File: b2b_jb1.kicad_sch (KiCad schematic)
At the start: 11 parts, among them SW1 SDA02H1SBDR

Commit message: edit README.md
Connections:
- net CLK3+ is gone; now on net CLK1+: JB1.95 (F16|B35|T0|AD0P|L1P)
- net CLK3- is gone; now on net CLK1-: JB1.93 (E16|B35|T0|AD0N|L1N)
- net CNV3+ is gone; now on net CNV1+: JB1.99 (H19|B35|T3|L19P)
- net CNV3- is gone; now on net CNV1-: JB1.97 (H20|B35|T3|VREF|L19N)
- net DA3+ is gone; now on net DA1+: JB1.81 (E15|B35|T0|DQS|AD1P|L3P)
- net DA3- is gone; now on net DA1-: JB1.79 (D15|B35|T0|DQS|AD1N|L3N)
- net DB3+ is gone; now on net DB1+: JB1.77 (F18|B35|T0|AD9P|L5P)
- net DB3- is gone; now on net DB1-: JB1.75 (E18|B35|T0|AD9N|L5N)
- net DCO3+ is gone; now on net DCO1+: JB1.87 (G17|B35|T0|L6P)
- net DCO3- is gone; now on net DCO1-: JB1.85 (F17|B35|T0|VREF|L6N)
- net CLK1+: no longer JB1.66 (C20|B35|T2|AD4N|SRCC|L14N)
- net CLK1-: no longer JB1.68 (D20|B35|T2|AD4P|SRCC|L14P)
- net CNV1+: no longer JB1.60 (B20|B35|T2|MRCC|L13N)
- net CNV1-: no longer JB1.62 (B19|B35|T2|MRCC|L13P)
- net DA1+: no longer JB1.76 (C19|B35|T1|MRCC|L12N)
- net DA1-: no longer JB1.78 (D18|B35|T1|MRCC|L12P)
- net DB1+: no longer JB1.82 (F19|B35|T3|AD6N|L20N)
- net DB1-: no longer JB1.84 (G19|B35|T3|AD6P|L20P)
- net DCO1+: no longer JB1.70 (G16|B35|T0|L4N)
- net DCO1-: no longer JB1.72 (G15|B35|T0|L4P)
- new net CLK0+: JB1.66 (C20|B35|T2|AD4N|SRCC|L14N)
- new net CLK0-: JB1.68 (D20|B35|T2|AD4P|SRCC|L14P)
- new net CNV0+: JB1.60 (B20|B35|T2|MRCC|L13N)
- new net CNV0-: JB1.62 (B19|B35|T2|MRCC|L13P)
- new net DA0+: JB1.76 (C19|B35|T1|MRCC|L12N)
- new net DA0-: JB1.78 (D18|B35|T1|MRCC|L12P)
- new net DB0+: JB1.82 (F19|B35|T3|AD6N|L20N)
- new net DB0-: JB1.84 (G19|B35|T3|AD6P|L20P)
- new net DCO0+: JB1.70 (G16|B35|T0|L4N)
- new net DCO0-: JB1.72 (G15|B35|T0|L4P)
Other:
- company: (none) -> NOIRLab
- title: (none) -> 4 channel ADC Module

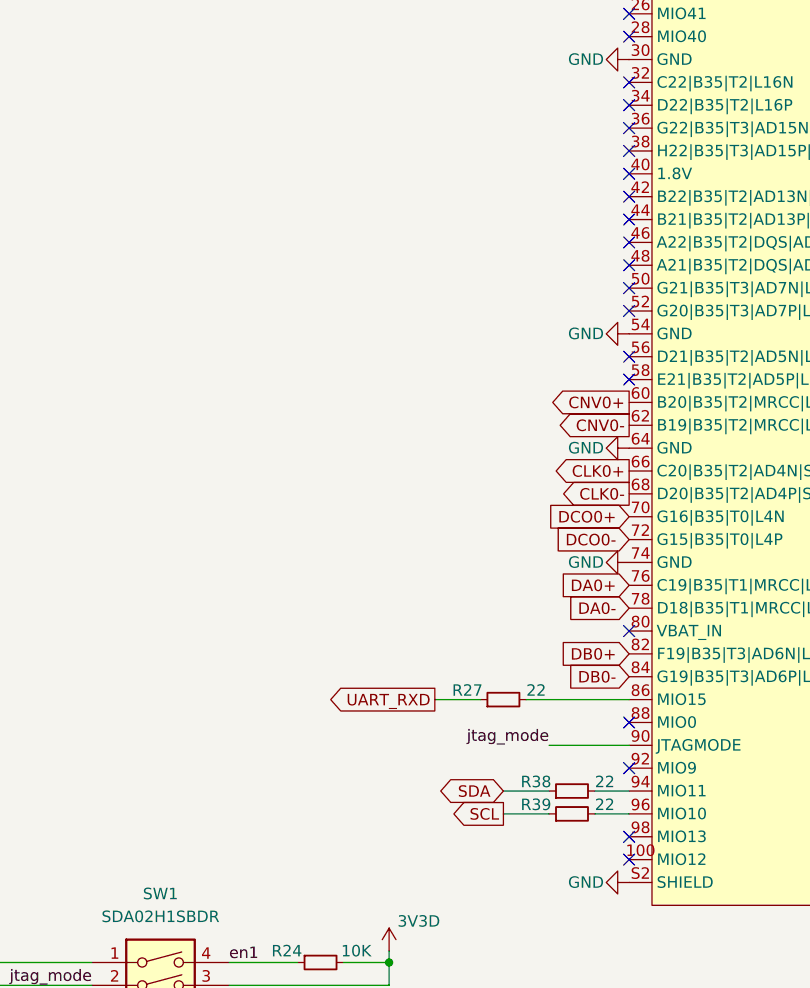
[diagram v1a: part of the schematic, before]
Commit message: Added clock sync and fix minor errors.
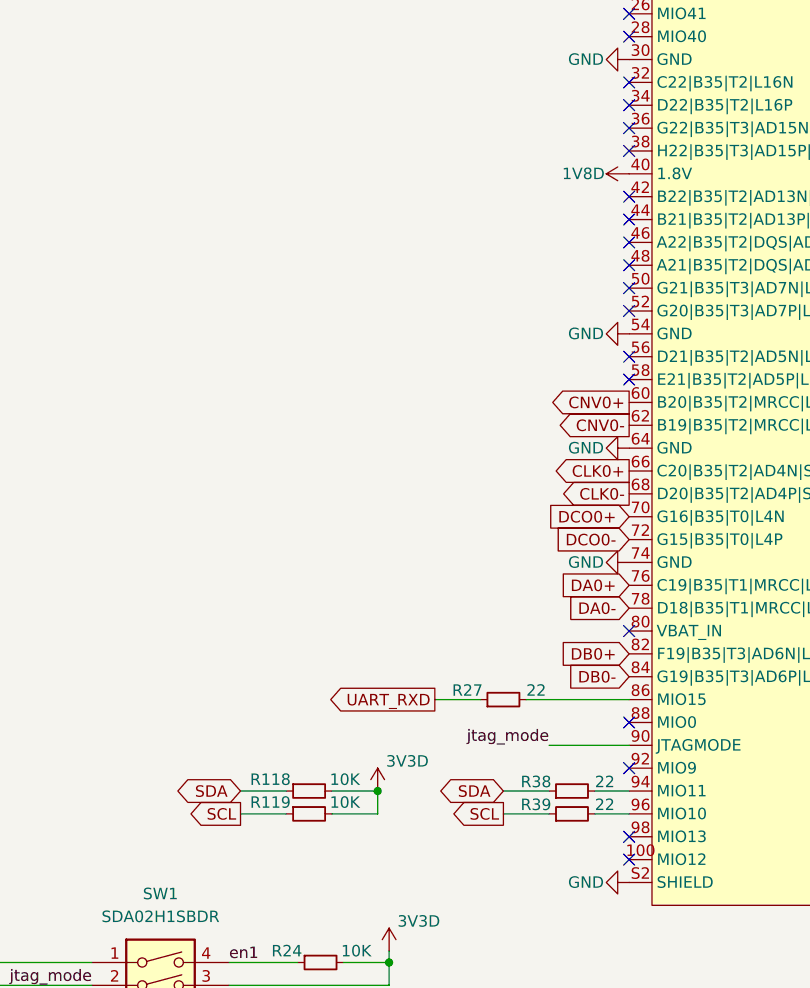
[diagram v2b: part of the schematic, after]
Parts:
- added R118, R119: 10K, Resistor_SMD:R_0603_1608Metric, symbol Device:R_Small
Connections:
- net 3V3D: now also R118.2, R119.2
- net SCL: now also R119.1
- net SDA: now also R118.1
- net 1V8D: now reaches JB1.40 (1.8V)
- no-connect marks 41 -> 40
